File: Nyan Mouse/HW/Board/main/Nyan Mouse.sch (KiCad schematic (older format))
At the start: 11 parts, among them M101 BATTBALANCE-2S, P101 Controller Connector, P102 CONN_4, P103 CONN_2, P104 CONN_2, U101 DRV8837, U102 DRV8837

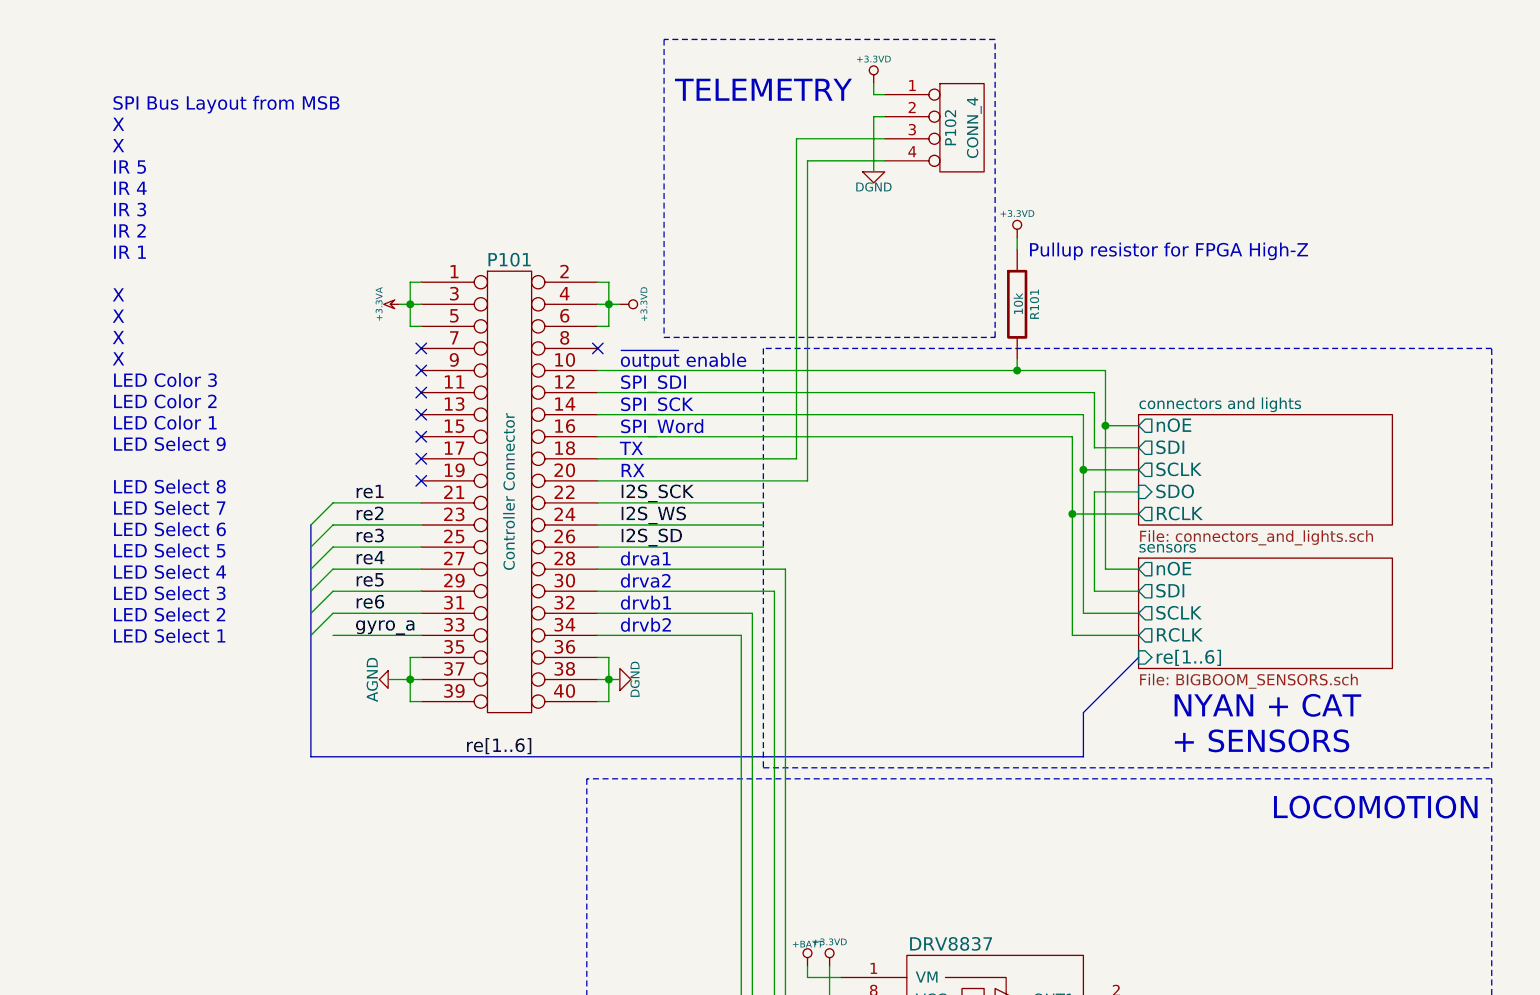
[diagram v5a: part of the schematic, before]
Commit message: Added DAC and amp.
Changed connector spec. for DAC and amp.  Sorry guys.
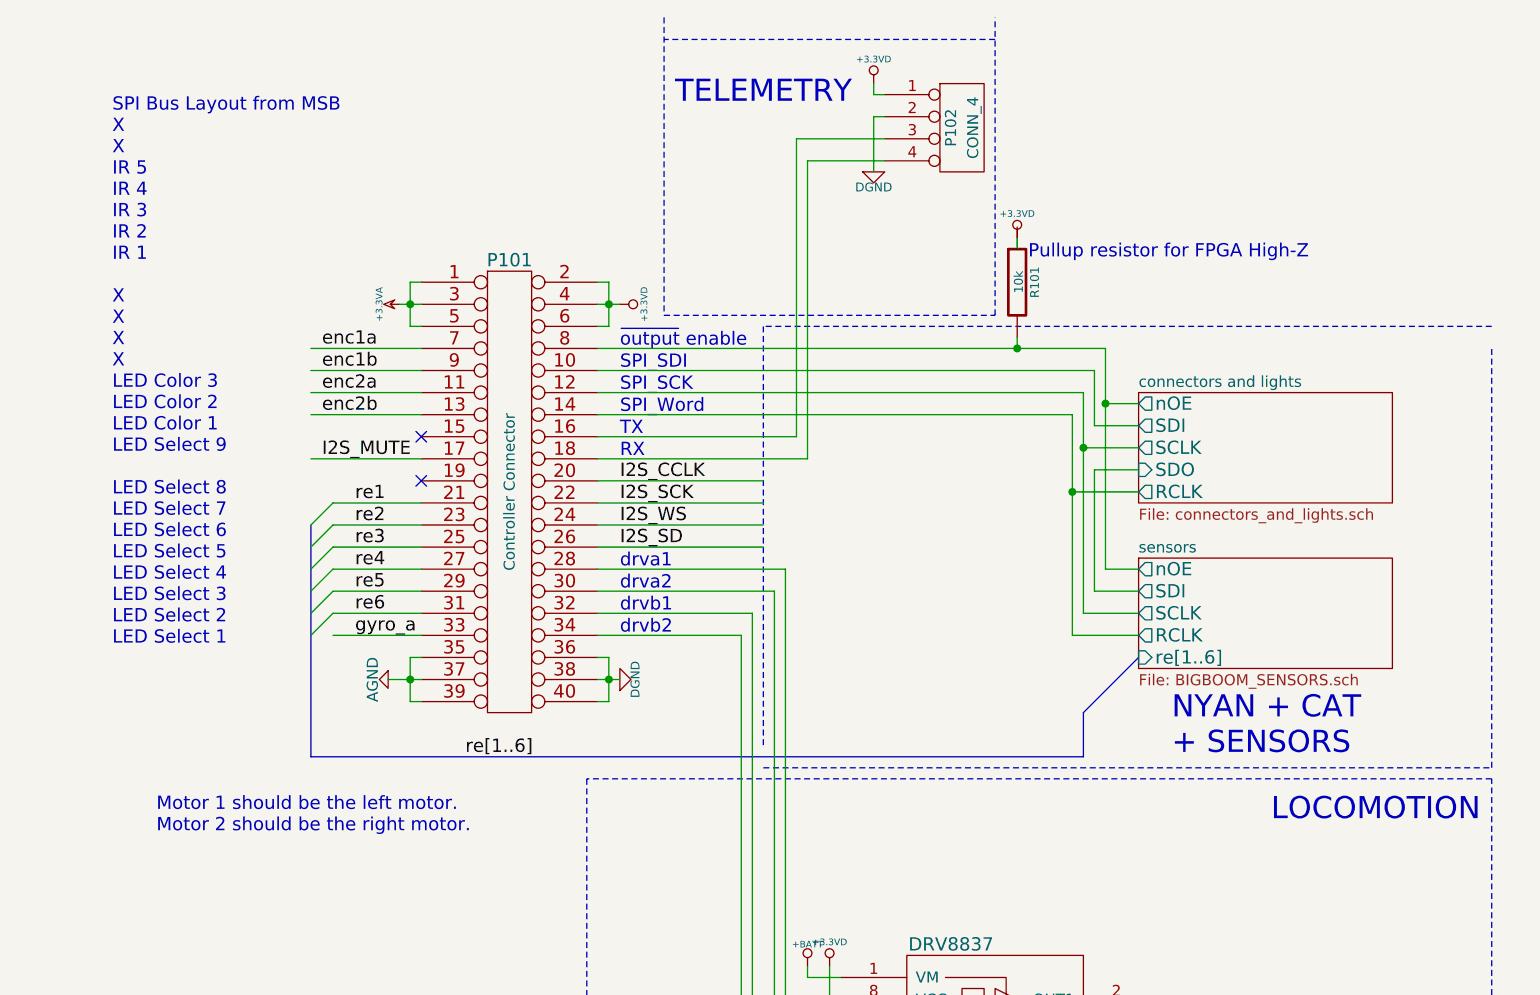
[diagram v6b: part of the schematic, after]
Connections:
- net labels added: I2S_CCLK, I2S_MUTE, enc1a, enc1b, enc2a, enc2b
- wire segments 112 -> 118
- no-connect marks 9 -> 3
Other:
- note added: "Motor 1 should be the left motor.\nMotor 2 should be the right motor."
- moved on the sheet: R101
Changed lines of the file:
@@
 LIBS:contrib
 LIBS:valves
-LIBS:3v3custom
-LIBS:adc128s052
-LIBS:altera_ep4ce15e22c
-LIBS:drv8837
-LIBS:JST-XH-BattBalance
-LIBS:lp3987
-LIBS:mic94345-4ycs
-LIBS:s25fl064p
-LIBS:SparkFun
-LIBS:stm32f103rx
-LIBS:tps6205x
 LIBS:Nyan Mouse-cache
 EELAYER 24 0
@@
 Sheet 1 5
 Title "Nyan Mouse"
-Date "24 apr 2014"
+Date "25 Apr 2014"
 Rev "Alpha"
 Comp "IEEE UCR"
@@
 "Connectors" for ground plane common reference point
 $Sheet
-S 8850 2200 1150 500
+S 8850 2100 1150 500
 U 5356EB92
 F0 "connectors and lights" 50
 F1 "connectors_and_lights.sch" 50
-F2 "SDI" O L 8850 2350 60
-F3 "nOE" O L 8850 2250 60
-F4 "RCLK" O L 8850 2650 60
-F5 "SCLK" O L 8850 2450 60
-F6 "SDO" I L 8850 2550 60
+F2 "SDI" O L 8850 2250 60
+F3 "nOE" O L 8850 2150 60
+F4 "RCLK" O L 8850 2550 60
+F5 "SCLK" O L 8850 2350 60
+F6 "SDO" I L 8850 2450 60
 $EndSheet
 $Comp
@@
 $EndComp
 Wire Wire Line
-	8850 2250 8700 2250
-Wire Wire Line
-	8700 2000 8700 2900
-Wire Wire Line
-	8700 2000 6400 2000
-Wire Wire Line
-	8850 2350 8650 2350
-Wire Wire Line
-	8650 2350 8650 2100
-Wire Wire Line
-	8650 2100 6400 2100
-Wire Wire Line
-	8850 2450 8600 2450
-Wire Wire Line
-	8600 2200 8600 3100
-Wire Wire Line
-	8850 2650 8550 2650
-Wire Wire Line
-	8550 2300 8550 3200
-Wire Wire Line
-	8550 2300 6400 2300
+	8850 2150 8700 2150
+Wire Wire Line
+	8700 1900 8700 2900
+Wire Wire Line
+	8700 1900 6400 1900
+Wire Wire Line
+	8850 2250 8650 2250
+Wire Wire Line
+	8650 2250 8650 2000
+Wire Wire Line
+	8650 2000 6400 2000
+Wire Wire Line
+	8850 2350 8600 2350
+Wire Wire Line
+	8600 2100 8600 3100
+Wire Wire Line
+	8550 2200 8550 3200
+Wire Wire Line
+	8550 2200 6400 2200
 $Comp
 L +3.3VD #PWR129
@@
 Wire Wire Line
 	8550 3200 8850 3200
-Connection ~ 8550 2650
 Wire Wire Line
 	8600 3100 8850 3100
-Connection ~ 8600 2450
-Wire Wire Line
-	8850 3000 8650 3000
-Wire Wire Line
-	8650 3000 8650 2550
-Wire Wire Line
-	8650 2550 8850 2550
+Connection ~ 8600 2350
+Wire Wire Line
+	8650 3000 8850 3000
+Wire Wire Line
+	8650 2450 8650 3000
 Wire Wire Line
 	8700 2900 8850 2900
-Connection ~ 8700 2250
+Connection ~ 8700 2150
 $Comp
 L R R101
 U 1 1 5357CE6B
-P 8300 1700
-F 0 "R101" V 8380 1700 40  0000 C CNN
-F 1 "10k" V 8307 1701 40  0000 C CNN
-F 2 "" V 8230 1700 30  0000 C CNN
-F 3 "" H 8300 1700 30  0000 C CNN
-	1    8300 1700
-	1    0    0    -1
-$EndComp
-Wire Wire Line
-	8600 2200 6400 2200
-Wire Wire Line
-	8300 1950 8300 2000
-Connection ~ 8300 2000
+P 8300 1600
+F 0 "R101" V 8380 1600 40  0000 C CNN
+F 1 "10k" V 8307 1601 40  0000 C CNN
+F 2 "" V 8230 1600 30  0000 C CNN
+F 3 "" H 8300 1600 30  0000 C CNN
+	1    8300 1600
+	1    0    0    -1
+$EndComp
+Wire Wire Line
+	8600 2100 6400 2100
+Wire Wire Line
+	8300 1850 8300 1900
+Connection ~ 8300 1900
+Text Notes 6500 1900 0    60   ~ 0
+~output enable
 Text Notes 6500 2000 0    60   ~ 0
-~output enable
+SPI_SDI
 Text Notes 6500 2100 0    60   ~ 0
-SPI_SDI
+SPI_SCK
 Text Notes 6500 2200 0    60   ~ 0
-SPI_SCK
-Text Notes 6500 2300 0    60   ~ 0
 SPI_Word
 Text Label 5300 2600 0    60   ~ 0
@@
 Wire Wire Line
 	7650 750  7650 700
+Text Notes 6500 2300 0    60   ~ 0
+TX
 Text Notes 6500 2400 0    60   ~ 0
-TX
-Text Notes 6500 2500 0    60   ~ 0
 RX
 NoConn ~ 5600 2300
@@
 Wire Wire Line
 	7050 3200 6400 3200
-NoConn ~ 5600 2200
-NoConn ~ 5600 2100
-NoConn ~ 5600 2000
-NoConn ~ 5600 1900
 Wire Wire Line
 	7350 1050 7700 1050
@@
 	6450 3300 6400 3300
 Wire Wire Line
-	7350 2500 6400 2500
-Wire Wire Line
-	6400 2400 7300 2400
+	7350 2400 6400 2400
+Wire Wire Line
+	7300 2300 6400 2300
 $Comp
 L CONN_20X2 P101
@@
 Wire Wire Line
 	6450 3500 6450 3300
-NoConn ~ 5600 2400
 NoConn ~ 5600 2500
 Wire Wire Line
@@
 Text Notes 7400 6650 0    60   ~ 0
 kevin, have you finished the layout for these yet?
-NoConn ~ 6400 1900
 Text Notes 3250 5400 0    60   ~ 0
 This is a todo section\n- Motor symbol & component\n- I2S DAC Symbol & Component\n- Audio Amplifier Symbol & Component\n- Speaker Wiring (Symbol & Component)\n- Gyro Symbol & Component
@@
 Text Notes 9450 4050 0    100  ~ 0
 LOCOMOTION
-Wire Wire Line
-	7300 2400 7300 950
-Wire Wire Line
-	7350 2500 7350 1050
-Wire Notes Line
-	6700 500  6700 1850
-Wire Notes Line
-	6700 1850 8200 1850
-Wire Notes Line
-	8200 1850 8200 500
+Wire Notes Line
+	6700 400  6700 1750
+Wire Notes Line
+	6700 1750 8200 1750
+Wire Notes Line
+	8200 1750 8200 400
 Wire Notes Line
 	8200 500  6700 500
@@
 TELEMETRY
 Wire Notes Line
-	7150 1900 7150 3800
+	7150 1800 7150 3700
 Wire Notes Line
 	7150 3800 10450 3800
@@
 	10450 3800 10450 1900
 Wire Notes Line
-	10450 1900 7150 1900
+	10450 1800 7150 1800
 Text Notes 9000 3750 0    100  ~ 0
 NYAN + CAT\n+ SENSORS
 Text Notes 8350 1500 0    60   ~ 0
 Pullup resistor for FPGA High-Z
+Wire Wire Line
+	5600 1900 5100 1900
+Wire Wire Line
+	5100 2000 5600 2000
+Wire Wire Line
+	5600 2100 5100 2100
+Wire Wire Line
+	5600 2200 5100 2200
+Text Label 5150 1900 0    60   ~ 0
+enc1a
+Text Label 5150 2000 0    60   ~ 0
+enc1b
+Text Label 5150 2100 0    60   ~ 0
+enc2a
+Text Label 5150 2200 0    60   ~ 0
+enc2b
+Text Notes 4400 4100 0    60   ~ 0
+Motor 1 should be the left motor.\nMotor 2 should be the right motor.
+Wire Wire Line
+	8850 2450 8650 2450
+Wire Wire Line
+	8550 2550 8850 2550
+Connection ~ 8550 2550
+Wire Wire Line
+	7300 950  7300 2300
+Wire Wire Line
+	7350 2400 7350 1050
+Wire Wire Line
+	6400 2500 7150 2500
+Text Label 6500 2500 0    60   ~ 0
+I2S_CCLK
+Text Label 5150 2400 0    60   ~ 0
+I2S_MUTE
+Wire Wire Line
+	5100 2400 5600 2400
 $EndSCHEMATC
